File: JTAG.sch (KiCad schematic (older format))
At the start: 45 parts, among them J11 MOLEX_87831-1420, J14 FTSH-105-01-L-DV-K-TR, Q17 BSS138LT1G, Q5 BSS138LT1G, U10 NC7SZ66P5X, U7 NC7SZ66P5X, U8 SN74AVC2T245RSWR, U9 SN74AVC2T245RSWR

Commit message: fixed bugs
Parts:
- J11: symbol AMC_FMC_Carrier-PcbDoc-rescue:MOLEX_87831-1420-MOLEX-AMC_FMC_Carrier-PcbDoc-rescue-AMC_FMC_Carrier-PcbDoc-rescue-AMC_FMC_Carrier-PcbDoc-rescue -> AMC_FMC_Carrier-PcbDoc-rescue:MOLEX_87831-1420-MOLEX-AMC_FMC_Carrier-PcbDoc-rescue-AMC_FMC_Carrier-PcbDoc-rescue-AMC_FMC_Carrier-PcbDoc-rescue-AMC_FMC_Carrier-PcbDoc-rescue
- J14: symbol AMC_FMC_Carrier-PcbDoc-rescue:Conn_ARM_JTAG_SWD_10-Connector-AMC_FMC_Carrier-PcbDoc-rescue-AMC_FMC_Carrier-PcbDoc-rescue-AMC_FMC_Carrier-PcbDoc-rescue -> AMC_FMC_Carrier-PcbDoc-rescue:Conn_ARM_JTAG_SWD_10-Connector-AMC_FMC_Carrier-PcbDoc-rescue-AMC_FMC_Carrier-PcbDoc-rescue-AMC_FMC_Carrier-PcbDoc-rescue-AMC_FMC_Carrier-PcbDoc-rescue
- U10, U7: symbol AMC_FMC_Carrier-PcbDoc-rescue:NC7SZ66P5X-Standard_Logic-AMC_FMC_Carrier-PcbDoc-rescue-AMC_FMC_Carrier-PcbDoc-rescue -> AMC_FMC_Carrier-PcbDoc-rescue:NC7SZ66P5X-Standard_Logic-AMC_FMC_Carrier-PcbDoc-rescue-AMC_FMC_Carrier-PcbDoc-rescue-AMC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
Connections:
- wire segments 138 -> 139
- no-connect marks 3 -> 2
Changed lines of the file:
@@
 	10050 4150 10500 4150
 $Comp
-L AMC_FMC_Carrier-PcbDoc-rescue:MOLEX_87831-1420-MOLEX-AMC_FMC_Carrier-PcbDoc-rescue-AMC_FMC_Carrier-PcbDoc-rescue-AMC_FMC_Carrier-PcbDoc-rescue J11
+L AMC_FMC_Carrier-PcbDoc-rescue:MOLEX_87831-1420-MOLEX-AMC_FMC_Carrier-PcbDoc-rescue-AMC_FMC_Carrier-PcbDoc-rescue-AMC_FMC_Carrier-PcbDoc-rescue-AMC_FMC_Carrier-PcbDoc-rescue J11
 U 1 1 5CB763C1
 P 4200 4700
@@
 EN_CON_JTAG
 $Comp
-L AMC_FMC_Carrier-PcbDoc-rescue:NC7SZ66P5X-Standard_Logic-AMC_FMC_Carrier-PcbDoc-rescue-AMC_FMC_Carrier-PcbDoc-rescue U7
+L AMC_FMC_Carrier-PcbDoc-rescue:NC7SZ66P5X-Standard_Logic-AMC_FMC_Carrier-PcbDoc-rescue-AMC_FMC_Carrier-PcbDoc-rescue-AMC_FMC_Carrier-PcbDoc-rescue U7
 U 1 1 5E17EE5A
 P 7600 1850
@@
 $EndComp
 $Comp
-L AMC_FMC_Carrier-PcbDoc-rescue:NC7SZ66P5X-Standard_Logic-AMC_FMC_Carrier-PcbDoc-rescue-AMC_FMC_Carrier-PcbDoc-rescue U10
+L AMC_FMC_Carrier-PcbDoc-rescue:NC7SZ66P5X-Standard_Logic-AMC_FMC_Carrier-PcbDoc-rescue-AMC_FMC_Carrier-PcbDoc-rescue-AMC_FMC_Carrier-PcbDoc-rescue U10
 U 1 1 5E17F12A
 P 5200 1850
@@
 MMC_TDI
 $Comp
-L AMC_FMC_Carrier-PcbDoc-rescue:Conn_ARM_JTAG_SWD_10-Connector-AMC_FMC_Carrier-PcbDoc-rescue-AMC_FMC_Carrier-PcbDoc-rescue-AMC_FMC_Carrier-PcbDoc-rescue J?
+L AMC_FMC_Carrier-PcbDoc-rescue:Conn_ARM_JTAG_SWD_10-Connector-AMC_FMC_Carrier-PcbDoc-rescue-AMC_FMC_Carrier-PcbDoc-rescue-AMC_FMC_Carrier-PcbDoc-rescue-AMC_FMC_Carrier-PcbDoc-rescue J?
 U 1 1 5E9BF6F9
 P 5550 4050
@@
 	1    0    0    -1
 $EndComp
-NoConn ~ 4400 4900
 $Comp
 L Resistors_SMD:R0402_0R_JUMPER R?
@@
 Text Label 9050 5400 0    50   ~ 10
 FMC1_TDI_R
+Wire Wire Line
+	4750 4900 4400 4900
+$Comp
+L power:+2V5 #PWR?
+U 1 1 5F980E3D
+P 4750 4900
+AR Path="/5C16BF8E/5F980E3D" Ref="#PWR?"  Part="1"
+AR Path="/5C16BF8E/5DB9B7E6/5F980E3D" Ref="#PWR?"  Part="1"
+AR Path="/5CA40231/5F980E3D" Ref="#PWR0798"  Part="1"
+F 0 "#PWR0798" H 4750 4750 50  0001 C CNN
+F 1 "+2V5" H 4765 5073 50  0000 C CNN
+F 2 "" H 4750 4900 50  0001 C CNN
+F 3 "" H 4750 4900 50  0001 C CNN
+	1    4750 4900
+	1    0    0    -1
+$EndComp
 $EndSCHEMATC

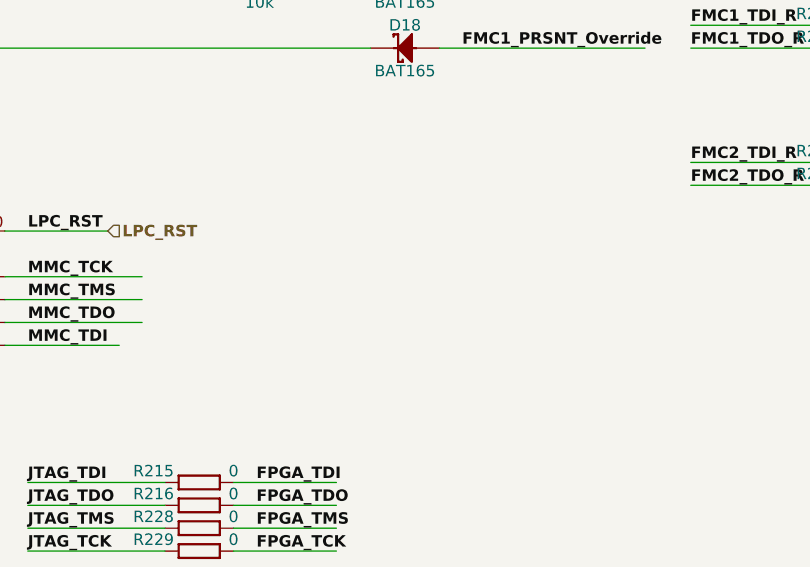
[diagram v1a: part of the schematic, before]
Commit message: added J9 connector compatibile with STM-NUCLEO programming header, added testpoints at MDIO
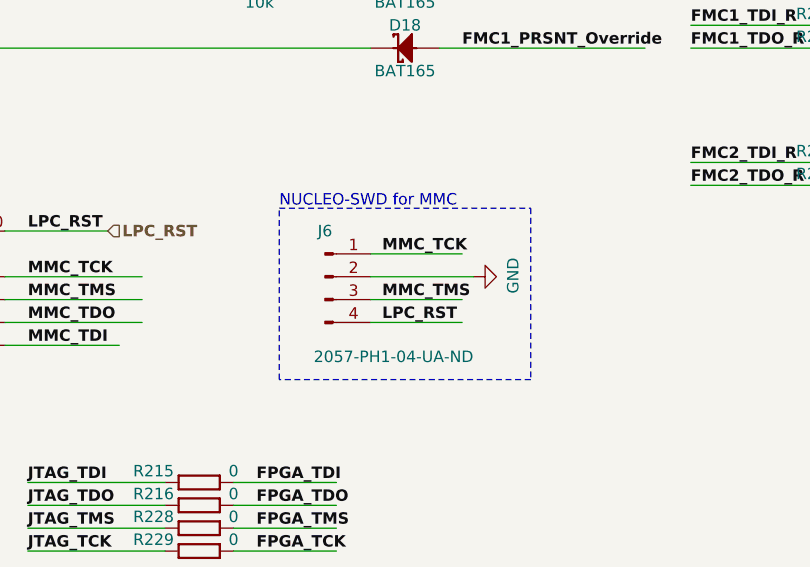
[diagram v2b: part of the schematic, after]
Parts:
- added J6: 2057-PH1-04-UA-ND, Connectors THD:SAMTEC_MTLW-104-07-L-S-250, symbol AMC_FMC_Carrier-PcbDoc-rescue:Conn_01x04_Male-Connector-AMC_FMC_Carrier-PcbDoc-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
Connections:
- wire segments 139 -> 143
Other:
- note added: "NUCLEO-SWD for MMC"
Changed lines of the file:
@@
 	1    0    0    -1
 $EndComp
+$Comp
+L AMC_FMC_Carrier-PcbDoc-rescue:Conn_01x04_Male-Connector-AMC_FMC_Carrier-PcbDoc-rescue-AMC_FMC_Carrier-PcbDoc-rescue-AMC_FMC_Carrier-PcbDoc-rescue-AMC_FMC_Carrier-PcbDoc-rescue J?
+U 1 1 5F8EAC42
+P 7450 3950
+AR Path="/5F8EAC42" Ref="J?"  Part="1"
+AR Path="/5C16BF8E/5F8EAC42" Ref="J?"  Part="1"
+AR Path="/5C16BF8E/5DB9B7E6/5F8EAC42" Ref="J?"  Part="1"
+AR Path="/5CA40231/5F8EAC42" Ref="J6"  Part="1"
+F 0 "J6" H 7450 4150 50  0000 C CNN
+F 1 "2057-PH1-04-UA-ND" H 7750 3600 50  0000 C CNN
+F 2 "Connectors THD:SAMTEC_MTLW-104-07-L-S-250" H 7450 3950 50  0001 C CNN
+F 3 "~" H 7450 3950 50  0001 C CNN
+F 4 "2057-PH1-04-UA-ND" H 7450 3950 50  0001 C CNN "Manufacturer Part Number"
+	1    7450 3950
+	1    0    0    -1
+$EndComp
+Text Label 7700 3850 0    50   ~ 10
+MMC_TCK
+Text Label 7700 4050 0    50   ~ 10
+MMC_TMS
+Text Label 7700 4150 0    50   ~ 10
+LPC_RST
+$Comp
+L power:GND #PWR?
+U 1 1 5F91C0FA
+P 8100 3950
+AR Path="/5BD32060/5F91C0FA" Ref="#PWR?"  Part="1"
+AR Path="/5BCEDA39/5F91C0FA" Ref="#PWR?"  Part="1"
+AR Path="/5CA40231/5F91C0FA" Ref="#PWR0825"  Part="1"
+F 0 "#PWR0825" H 8100 3700 50  0001 C CNN
+F 1 "GND" H 8105 3777 50  0000 C CNN
+F 2 "" H 8100 3950 50  0001 C CNN
+F 3 "" H 8100 3950 50  0001 C CNN
+	1    8100 3950
+	0    -1   -1   0
+$EndComp
+Wire Wire Line
+	8050 3850 7650 3850
+Wire Wire Line
+	8100 3950 7650 3950
+Wire Wire Line
+	7650 4050 8050 4050
+Wire Wire Line
+	8050 4150 7650 4150
+Wire Notes Line
+	7250 3650 8350 3650
+Wire Notes Line
+	8350 3650 8350 4400
+Wire Notes Line
+	8350 4400 7250 4400
+Wire Notes Line
+	7250 4400 7250 3650
+Text Notes 7250 3650 0    50   ~ 0
+NUCLEO-SWD for MMC
 $EndSCHEMATC

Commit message: Automated edit to move cache / rescue symbols to actual eeschem library
Results of running dissect_lib3.py, not posted here
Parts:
- J11: symbol AMC_FMC_Carrier-PcbDoc-rescue:MOLEX_87831-1420-MOLEX-AMC_FMC_Carrier-PcbDoc-rescue-AMC_FMC_Carrier-PcbDoc-rescue-AMC_FM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 -> marble_misc:MOLEX_87831-1420-MOLEX
- J14: symbol AMC_FMC_Carrier-PcbDoc-rescue:Conn_ARM_JTAG_SWD_10-Connector-AMC_FMC_Carrier-PcbDoc-rescue-AMC_FMC_Carrier-PcbDoc-rescu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 -> marble_misc:Conn_ARM_JTAG_SWD_10-Connector
- J6: symbol AMC_FMC_Carrier-PcbDoc-rescue:Conn_01x04_Male-Connector-AMC_FMC_Carrier-PcbDoc-rescue-AMC_FMC_Carrier-PcbDoc-rescue-AMC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 -> marble_misc:Conn_01x04_Male-Connector
- U10, U7: symbol AMC_FMC_Carrier-PcbDoc-rescue:NC7SZ66P5X-Standard_Logic-AMC_FMC_Carrier-PcbDoc-rescue-AMC_FMC_Carrier-PcbDoc-rescue-AMC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 -> marble_misc:NC7SZ66P5X-Standard_Logic
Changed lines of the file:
@@
 	10050 4150 10500 4150
 $Comp
-L AMC_FMC_Carrier-PcbDoc-rescue:MOLEX_87831-1420-MOLEX-AMC_FMC_Carrier-PcbDoc-rescue-AMC_FMC_Carrier-PcbDoc-rescue-AMC_FMC_Carrier-PcbDoc-rescue-AMC_FMC_Carrier-PcbDoc-rescue J11
+L marble_misc:MOLEX_87831-1420-MOLEX J11
 U 1 1 5CB763C1
 P 4200 4700
@@
 EN_CON_JTAG
 $Comp
-L AMC_FMC_Carrier-PcbDoc-rescue:NC7SZ66P5X-Standard_Logic-AMC_FMC_Carrier-PcbDoc-rescue-AMC_FMC_Carrier-PcbDoc-rescue-AMC_FMC_Carrier-PcbDoc-rescue U7
+L marble_misc:NC7SZ66P5X-Standard_Logic U7
 U 1 1 5E17EE5A
 P 7600 1850
@@
 $EndComp
 $Comp
-L AMC_FMC_Carrier-PcbDoc-rescue:NC7SZ66P5X-Standard_Logic-AMC_FMC_Carrier-PcbDoc-rescue-AMC_FMC_Carrier-PcbDoc-rescue-AMC_FMC_Carrier-PcbDoc-rescue U10
+L marble_misc:NC7SZ66P5X-Standard_Logic U10
 U 1 1 5E17F12A
 P 5200 1850
@@
 MMC_TDI
 $Comp
-L AMC_FMC_Carrier-PcbDoc-rescue:Conn_ARM_JTAG_SWD_10-Connector-AMC_FMC_Carrier-PcbDoc-rescue-AMC_FMC_Carrier-PcbDoc-rescue-AMC_FMC_Carrier-PcbDoc-rescue-AMC_FMC_Carrier-PcbDoc-rescue J?
+L marble_misc:Conn_ARM_JTAG_SWD_10-Connector J?
 U 1 1 5E9BF6F9
 P 5550 4050
@@
 $EndComp
 $Comp
-L power2:+3.3P #PWR?
+L power:+3.3P #PWR?
 U 1 1 5D430167
 P 5450 1050
@@
 $EndComp
 $Comp
-L power2:+3.3P #PWR?
+L power:+3.3P #PWR?
 U 1 1 5D4357CC
 P 5900 1050
@@
 $EndComp
 $Comp
-L power2:+3.3P #PWR?
+L power:+3.3P #PWR?
 U 1 1 5D440498
 P 5550 3450
@@
 $EndComp
 $Comp
-L power2:+3.3P #PWR?
+L power:+3.3P #PWR?
 U 1 1 5D445B1A
 P 6000 2050
@@
 $EndComp
 $Comp
-L power2:+3.3P #PWR?
+L power:+3.3P #PWR?
 U 1 1 5D460C62
 P 8400 2050
@@
 $EndComp
 $Comp
-L power2:+3.3P #PWR?
+L power:+3.3P #PWR?
 U 1 1 5D46B90D
 P 2300 5350
@@
 $EndComp
 $Comp
-L AMC_FMC_Carrier-PcbDoc-rescue:Conn_01x04_Male-Connector-AMC_FMC_Carrier-PcbDoc-rescue-AMC_FMC_Carrier-PcbDoc-rescue-AMC_FMC_Carrier-PcbDoc-rescue-AMC_FMC_Carrier-PcbDoc-rescue J?
+L marble_misc:Conn_01x04_Male-Connector J?
 U 1 1 5F8EAC42
 P 7450 3950

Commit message: More consistent attributes for LEDs and BSS138
Should match Marble-Mini
Fewer complaints from KiBoM
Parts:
- Q17, Q5: HelpURL \\\\cern.ch\\dfs\\Applications\\Altium\\Datasheets\\BSS139.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 -> \\\\cern.ch\\dfs\\Applications\\Altium\\Datasheets\\BSS138L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; Library Name ICs And Semiconductors.DbLib -> ICs And Semiconductors SMD
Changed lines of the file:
@@
 F 1 "BSS138LT1G" H 2319 5655 50  0000 L CNN
 F 2 "ICs And Semiconductors SMD:SOT95P240X110-3N" H 2000 4440 60  0001 L CNN
-F 3 "\\\\cern.ch\\dfs\\Applications\\Altium\\Datasheets\\BSS139.pdf" H 2000 5160 60  0001 L CNN
+F 3 "\\\\cern.ch\\dfs\\Applications\\Altium\\Datasheets\\BSS138LT1G.pdf" H 2000 5160 60  0001 L CNN
 F 4 "BSS138LT1G" H 2000 5070 60  0001 L CNN "Part Number"
 F 5 "N-MOSFET-D 1G 2S 3D" H 2000 4980 60  0001 L CNN "Library Ref"
@@
 F 27 "PcbLib\\ICs And Semiconductors SMD.PcbLib" H 2000 2910 60  0001 L CNN "Footprint Path"
 F 28 "SOT95P240X110-3N" H 2000 2820 60  0001 L CNN "Footprint Ref"
-F 29 "\\\\cern.ch\\dfs\\Applications\\Altium\\Datasheets\\BSS139.pdf" H 2000 2730 60  0001 L CNN "HelpURL"
+F 29 "\\\\cern.ch\\dfs\\Applications\\Altium\\Datasheets\\BSS138LT1G.pdf" H 2000 2730 60  0001 L CNN "HelpURL"
 F 30 "~~" H 2000 2640 60  0001 L CNN "ComponentLink1URL"
 F 31 " " H 2000 2550 60  0001 L CNN "ComponentLink1Description"
@@
 F 35 "03/23/09 00:00:00" H 2000 2190 60  0001 L CNN "CreateDate"
 F 36 "03/23/09 00:00:00" H 2000 2100 60  0001 L CNN "LatestRevisionDate"
-F 37 "ICs And Semiconductors.DbLib" H 2000 2010 60  0001 L CNN "Library Name"
+F 37 "ICs And Semiconductors SMD" H 2000 2010 60  0001 L CNN "Library Name"
 F 38 "This work is licensed under the Creative Commons CC-BY-SA 4.0 License. To the extent that circuit schematics that use Licensed Material can be considered to be ‘Adapted Material’, then the copyright holder waives article 3.b of the license with respect to these schematics." H 2000 1920 60  0001 L CNN "License"
 F 39 "Transistors" H 2000 5650 50  0001 C CNN "Database Table Name"
@@
 F 1 "BSS138LT1G" H 2769 6455 50  0000 L CNN
 F 2 "ICs And Semiconductors SMD:SOT95P240X110-3N" H 2450 5240 60  0001 L CNN
-F 3 "\\\\cern.ch\\dfs\\Applications\\Altium\\Datasheets\\BSS139.pdf" H 2450 5960 60  0001 L CNN
+F 3 "\\\\cern.ch\\dfs\\Applications\\Altium\\Datasheets\\BSS138LT1G.pdf" H 2450 5960 60  0001 L CNN
 F 4 "BSS138LT1G" H 2450 5870 60  0001 L CNN "Part Number"
 F 5 "N-MOSFET-D 1G 2S 3D" H 2450 5780 60  0001 L CNN "Library Ref"
@@
 F 27 "PcbLib\\ICs And Semiconductors SMD.PcbLib" H 2450 3710 60  0001 L CNN "Footprint Path"
 F 28 "SOT95P240X110-3N" H 2450 3620 60  0001 L CNN "Footprint Ref"
-F 29 "\\\\cern.ch\\dfs\\Applications\\Altium\\Datasheets\\BSS139.pdf" H 2450 3530 60  0001 L CNN "HelpURL"
+F 29 "\\\\cern.ch\\dfs\\Applications\\Altium\\Datasheets\\BSS138LT1G.pdf" H 2450 3530 60  0001 L CNN "HelpURL"
 F 30 "~~" H 2450 3440 60  0001 L CNN "ComponentLink1URL"
 F 31 " " H 2450 3350 60  0001 L CNN "ComponentLink1Description"
@@
 F 35 "03/23/09 00:00:00" H 2450 2990 60  0001 L CNN "CreateDate"
 F 36 "03/23/09 00:00:00" H 2450 2900 60  0001 L CNN "LatestRevisionDate"
-F 37 "ICs And Semiconductors.DbLib" H 2450 2810 60  0001 L CNN "Library Name"
+F 37 "ICs And Semiconductors SMD" H 2450 2810 60  0001 L CNN "Library Name"
 F 38 "This work is licensed under the Creative Commons CC-BY-SA 4.0 License. To the extent that circuit schematics that use Licensed Material can be considered to be ‘Adapted Material’, then the copyright holder waives article 3.b of the license with respect to these schematics." H 2450 2720 60  0001 L CNN "License"
 F 39 "Transistors" H 2450 6450 50  0001 C CNN "Database Table Name"

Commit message: Progress on the BOM
Fill in many Manufacturer fields
Move dnf flag from Y1 to Y2
Manufacturer Part Number changes for Y1 D8 J6 J9
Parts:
- J14: Manufacturer (none) -> SULLINS
- J6: Manufacturer (none) -> Adam Tech; Manufacturer Part Number 2057-PH1-04-UA-ND -> PH1-04-UA
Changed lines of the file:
@@
 F 3 "http://infocenter.arm.com/help/topic/com.arm.doc.faqs/attached/13634/cortex_debug_connectors.pdf" V 5200 2800 50  0001 C CNN
 F 4 "GRPB052VWQP-RC" H 5550 4050 50  0001 C CNN "Manufacturer Part Number"
+F 5 "SULLINS" H 5550 4050 50  0001 C CNN "Manufacturer"
 	1    5550 4050
 	1    0    0    -1
@@
 F 2 "Connectors THD:SAMTEC_MTLW-104-07-L-S-250" H 7450 3950 50  0001 C CNN
 F 3 "~" H 7450 3950 50  0001 C CNN
-F 4 "2057-PH1-04-UA-ND" H 7450 3950 50  0001 C CNN "Manufacturer Part Number"
+F 4 "PH1-04-UA" H 7450 3950 50  0001 C CNN "Manufacturer Part Number"
+F 5 "Adam Tech" H 7450 3950 50  0001 C CNN "Manufacturer"
 	1    7450 3950
 	1    0    0    -1

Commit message: Stop saying that 2-pin devices have "2.0000000000000000e+00" pins
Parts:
- C193, C211, C212, C213, C214, C358, C359: Pin Count 2.0000000000000000e+00 -> 2
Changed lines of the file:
@@
 F 9 "Standard" H 2300 3360 60  0001 L CNN "Component Kind"
 F 10 "Standard" H 2300 3270 60  0001 L CNN "Component Type"
-F 11 "2.0000000000000000e+00" H 2300 3090 60  0001 L CNN "Pin Count"
+F 11 "2" H 2300 3090 60  0001 L CNN "Pin Count"
 F 12 "PcbLib\\Capacitors SMD.PcbLib" H 2300 3000 60  0001 L CNN "Footprint Path"
 F 13 "CAPC0603X33N" H 2300 2910 60  0001 L CNN "Footprint Ref"
@@
 F 9 "Standard" H 2750 3360 60  0001 L CNN "Component Kind"
 F 10 "Standard" H 2750 3270 60  0001 L CNN "Component Type"
-F 11 "2.0000000000000000e+00" H 2750 3090 60  0001 L CNN "Pin Count"
+F 11 "2" H 2750 3090 60  0001 L CNN "Pin Count"
 F 12 "PcbLib\\Capacitors SMD.PcbLib" H 2750 3000 60  0001 L CNN "Footprint Path"
 F 13 "CAPC0603X33N" H 2750 2910 60  0001 L CNN "Footprint Ref"
@@
 F 9 "Standard" H 2300 1410 60  0001 L CNN "Component Kind"
 F 10 "Standard" H 2300 1320 60  0001 L CNN "Component Type"
-F 11 "2.0000000000000000e+00" H 2300 1140 60  0001 L CNN "Pin Count"
+F 11 "2" H 2300 1140 60  0001 L CNN "Pin Count"
 F 12 "PcbLib\\Capacitors SMD.PcbLib" H 2300 1050 60  0001 L CNN "Footprint Path"
 F 13 "CAPC0603X33N" H 2300 960 60  0001 L CNN "Footprint Ref"
@@
 F 9 "Standard" H 2750 1410 60  0001 L CNN "Component Kind"
 F 10 "Standard" H 2750 1320 60  0001 L CNN "Component Type"
-F 11 "2.0000000000000000e+00" H 2750 1140 60  0001 L CNN "Pin Count"
+F 11 "2" H 2750 1140 60  0001 L CNN "Pin Count"
 F 12 "PcbLib\\Capacitors SMD.PcbLib" H 2750 1050 60  0001 L CNN "Footprint Path"
 F 13 "CAPC0603X33N" H 2750 960 60  0001 L CNN "Footprint Ref"
@@
 F 9 "Standard" H 5450 5110 60  0001 L CNN "Component Kind"
 F 10 "Standard" H 5450 5020 60  0001 L CNN "Component Type"
-F 11 "2.0000000000000000e+00" H 5450 4840 60  0001 L CNN "Pin Count"
+F 11 "2" H 5450 4840 60  0001 L CNN "Pin Count"
 F 12 "PcbLib\\Capacitors SMD.PcbLib" H 5450 4750 60  0001 L CNN "Footprint Path"
 F 13 "CAPC0603X33N" H 5450 4660 60  0001 L CNN "Footprint Ref"
@@
 F 9 "Standard" H 5450 160 60  0001 L CNN "Component Kind"
 F 10 "Standard" H 5450 70  60  0001 L CNN "Component Type"
-F 11 "2.0000000000000000e+00" H 5450 -110 60  0001 L CNN "Pin Count"
+F 11 "2" H 5450 -110 60  0001 L CNN "Pin Count"
 F 12 "PcbLib\\Capacitors SMD.PcbLib" H 5450 -200 60  0001 L CNN "Footprint Path"
 F 13 "CAPC0603X33N" H 5450 -290 60  0001 L CNN "Footprint Ref"
@@
 F 9 "Standard" H 5900 160 60  0001 L CNN "Component Kind"
 F 10 "Standard" H 5900 70  60  0001 L CNN "Component Type"
-F 11 "2.0000000000000000e+00" H 5900 -110 60  0001 L CNN "Pin Count"
+F 11 "2" H 5900 -110 60  0001 L CNN "Pin Count"
 F 12 "PcbLib\\Capacitors SMD.PcbLib" H 5900 -200 60  0001 L CNN "Footprint Path"
 F 13 "CAPC0603X33N" H 5900 -290 60  0001 L CNN "Footprint Ref"

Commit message: Convert "~" and "~~" in .sch and .lib files to " "
cf. commit ef029e49 in Marble-Mini, May 21 2020
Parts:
- C193, C211, C212, C213, C214, C358, C359: ComponentHeight ~~ -> (none); PackageDescription ~~ -> (none); PressFit ~~ -> (none); Sense Comment ~~ -> (none); Status Comment ~~ -> (none)
- D14, D15, D17, D18, U10, U7: ComponentLink1Description ~~ -> (none); ComponentLink1URL ~~ -> (none); ComponentLink2Description ~~ -> (none); ComponentLink2URL ~~ -> (none); Sense Comment ~~ -> (none); Status ~~ -> (none); Status Comment ~~ -> (none)
- J11: Case ~~ -> (none); Comment ~~ -> (none); ComponentLink1Description ~~ -> (none); ComponentLink1URL ~~ -> (none); ComponentLink2Description ~~ -> (none); ComponentLink2URL ~~ -> (none); Device ~~ -> (none); PackageDescription ~~ -> (none); SCEM ~~ -> (none); Sense Comment ~~ -> (none); Status Comment ~~ -> (none)
- Q17, Q5: ComponentLink1URL ~~ -> (none); ComponentLink2URL ~~ -> (none)
- R131, R166, R246, R276, R63: ComponentHeight ~~ -> (none); PackageDescription ~~ -> (none); Sense Comment ~~ -> (none); Status Comment ~~ -> (none); Voltage ~~ -> (none)
- R215, R216, R228, R229, R230, R231, R232, R233, R237, R238, R239, R240, R241, R242, R275, R277, R278, R279, R280, R289, R290: ComponentHeight ~~ -> (none); PackageDescription ~~ -> (none); Power ~~ -> (none); Sense Comment ~~ -> (none); Status Comment ~~ -> (none); TC ~~ -> (none); Tolerance ~~ -> (none); Voltage ~~ -> (none)
- U8, U9: ComponentLink1Description ~~ -> (none); ComponentLink1URL ~~ -> (none); ComponentLink2Description ~~ -> (none); ComponentLink2URL ~~ -> (none); Sense Comment ~~ -> (none); Status Comment ~~ -> (none)

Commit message: Remove some un-helpful attributes
Pole4
SCEM
Footprint Library
Database Table Name
HelpURL
ComponentLink1URL
ComponentLink2URL
CreateDate1
LatestRevisionDate1

cf. commits 8f7a3695 c705ea46 d128e165 ffe4a47d in Marble-Mini, May 21 2020
Cuts number of attrib_lint complaints in half, to 2334.
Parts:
- C193, C211, C212, C213, C214, C358, C359: HelpURL \\\\cern.ch\\dfs\\Applications\\Altium\\Datasheets\\CC0201_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 -> (none)
- D14, D15, D17, D18: ComponentLink1URL (none) -> (none); ComponentLink2URL (none) -> (none); HelpURL \\\\cern.ch\\dfs\\Applications\\Altium\\Datasheets\\BAT165.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 -> (none)
- J11: ComponentLink1URL (none) -> (none); ComponentLink2URL (none) -> (none); HelpURL \\\\cern.ch\\dfs\\Applications\\Altium\\Datasheets\\MOLEX_8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 -> (none); Pole4 Milli-Grid™ -> (none); SCEM (none) -> (none)
- Q17, Q5: ComponentLink1URL (none) -> (none); ComponentLink2URL (none) -> (none); Database Table Name Transistors -> (none); Footprint Library ICs And Semiconductors SMD -> (none); HelpURL \\\\cern.ch\\dfs\\Applications\\Altium\\Datasheets\\BSS138L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 -> (none); SCEM (none) -> (none)
- R131, R166, R215, R216, R228, R229, R230, R231, R232, R233, R237, R238, R239, R240, R241, R242, R246, R275, R276, R277, R278, R279, R280, R289, R290, R63: HelpURL \\\\cern.ch\\dfs\\Applications\\Altium\\Datasheets\\R0402_P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 -> (none)
- U10, U7: ComponentLink1URL (none) -> (none); ComponentLink2URL (none) -> (none); HelpURL \\\\cern.ch\\dfs\\Applications\\Altium\\Datasheets\\NC7SZ66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 -> (none)
- U8, U9: ComponentLink1URL (none) -> (none); ComponentLink2URL (none) -> (none); HelpURL \\\\cern.ch\\dfs\\Applications\\Altium\\Datasheets\\SN74AVC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 -> (none)
